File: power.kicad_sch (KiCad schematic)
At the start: 76 parts, among them J5 VJ1, Q1 BC857, Q2 2N7002, U1 LFE5U-85F-6BG381C, U3 TLV62569DBV, U4 TLV62569DBV, U5 TLV62569DBV

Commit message: updating part numbers across schematcs
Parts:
- C1, C11, C12, C3, C4, C5, C7, C8, C9: MPN CC0805ZKY5V5BB226 -> CC0805ZKY5V5BB226
- C26, C27, C28, C29, C30, C31, C32, C48, C49, C50, C51, C53: MPN CX0603MRX7R8BB223 -> CC0603JRX7R8BB223
- D10, D13, D14, D16, D17, D27: MPN 1N4148WS -> 1N4148WS
- R10: Digikey (none) -> 13-AC0603FR-07130RLCT-ND; MPN (none) -> 13-AC0603FR-07130RLCT-ND
- R6, R66, R8: Digikey (none) -> 13-AC0603FR-071K1LCT-ND; MPN (none) -> 13-AC0603FR-071K1LCT-ND
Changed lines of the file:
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@@
 			)
 		)
-		(property "MPN" "CC0805ZKY5V5BB226 "
+		(property "MPN" "CC0805ZKY5V5BB226"
 			(at 187.96 93.98 0)
 			(effects
@@
 			)
 		)
-		(property "MPN" "CC0805ZKY5V5BB226 "
+		(property "MPN" "CC0805ZKY5V5BB226"
 			(at 248.92 83.82 0)
 			(effects
@@
 			)
 		)
-		(property "MPN" "CC0805ZKY5V5BB226 "
+		(property "MPN" "CC0805ZKY5V5BB226"
 			(at 257.81 83.82 0)
 			(effects
@@
 			)
 		)
-		(property "MPN" "CC0805ZKY5V5BB226 "
+		(property "MPN" "CC0805ZKY5V5BB226"
 			(at 187.96 154.94 0)
 			(effects
@@
 			)
 		)
-		(property "MPN" "CC0805ZKY5V5BB226 "
+		(property "MPN" "CC0805ZKY5V5BB226"
 			(at 248.92 144.78 0)
 			(effects
@@
 			)
 		)
-		(property "MPN" "CC0805ZKY5V5BB226 "
+		(property "MPN" "CC0805ZKY5V5BB226"
 			(at 257.81 144.78 0)
 			(effects
@@
 			)
 		)
-		(property "MPN" "CC0805ZKY5V5BB226 "
+		(property "MPN" "CC0805ZKY5V5BB226"
 			(at 187.96 124.46 0)
 			(effects
@@
 			)
 		)
-		(property "MPN" "CC0805ZKY5V5BB226 "
+		(property "MPN" "CC0805ZKY5V5BB226"
 			(at 248.92 114.3 0)
 			(effects
@@
 			)
 		)
-		(property "MPN" "CC0805ZKY5V5BB226 "
+		(property "MPN" "CC0805ZKY5V5BB226"
 			(at 257.81 114.3 0)
 			(effects
@@
 			)
 		)
-		(property "MPN" "1N4148WS "
+		(property "MPN" "1N4148WS"
 			(at 109.22 107.95 0)
 			(effects
@@
 			)
 		)
+		(property "Digikey" "13-AC0603FR-071K1LCT-ND"
+			(at 86.36 95.25 90)
+			(effects
+				(font
+					(size 1.27 1.27)
+				)
+				(hide yes)
+			)
+		)
+		(property "MPN" "13-AC0603FR-071K1LCT-ND"
+			(at 86.36 95.25 90)
+			(effects
+				(font
+					(size 1.27 1.27)
+				)
+				(hide yes)
+			)
+		)
 		(pin "1"
 		)
@@
 			)
 		)
+		(property "Digikey" "13-AC0603FR-071K1LCT-ND"
+			(at 104.14 132.08 90)
+			(effects
+				(font
+					(size 1.27 1.27)
+				)
+				(hide yes)
+			)
+		)
+		(property "MPN" "13-AC0603FR-071K1LCT-ND"
+			(at 104.14 132.08 90)
+			(effects
+				(font
+					(size 1.27 1.27)
+				)
+				(hide yes)
+			)
+		)
 		(pin "1"
 		)
@@
 			)
 		)
-		(property "MPN" "1N4148WS "
+		(property "MPN" "1N4148WS"
 			(at 102.87 107.95 0)
 			(effects
@@
 			)
 		)
-		(property "MPN" "1N4148WS "
+		(property "MPN" "1N4148WS"
 			(at 86.36 137.16 0)
 			(effects
@@
 			)
 		)
-		(property "MPN" "1N4148WS "
+		(property "MPN" "1N4148WS"
 			(at 73.66 100.33 0)
 			(effects
@@
 			)
 		)
-		(property "MPN" "1N4148WS "
+		(property "MPN" "1N4148WS"
 			(at 80.01 105.41 0)
 			(effects
@@
 			)
 		)
+		(property "Digikey" "13-AC0603FR-07130RLCT-ND"
+			(at 68.58 125.73 90)
+			(effects
+				(font
+					(size 1.27 1.27)
+				)
+				(hide yes)
+			)
+		)
+		(property "MPN" "13-AC0603FR-07130RLCT-ND"
+			(at 68.58 125.73 90)
+			(effects
+				(font
+					(size 1.27 1.27)
+				)
+				(hide yes)
+			)
+		)
 		(pin "1"
 		)
@@
 			)
 		)
-		(property "MPN" "CX0603MRX7R8BB223"
+		(property "MPN" "CC0603JRX7R8BB223"
 			(at 153.67 120.65 0)
 			(effects
@@
 			)
 		)
-		(property "MPN" "CX0603MRX7R8BB223"
+		(property "MPN" "CC0603JRX7R8BB223"
 			(at 139.7 82.55 0)
 			(effects
@@
 			)
 		)
-		(property "MPN" "CX0603MRX7R8BB223"
+		(property "MPN" "CC0603JRX7R8BB223"
 			(at 146.05 82.55 0)
 			(effects
@@
 			)
 		)
-		(property "MPN" "CX0603MRX7R8BB223"
+		(property "MPN" "CC0603JRX7R8BB223"
 			(at 139.7 101.6 0)
 			(effects
@@
 			)
 		)
-		(property "MPN" "CX0603MRX7R8BB223"
+		(property "MPN" "CC0603JRX7R8BB223"
 			(at 146.05 101.6 0)
 			(effects
@@
 			)
 		)
-		(property "MPN" "CX0603MRX7R8BB223"
+		(property "MPN" "CC0603JRX7R8BB223"
 			(at 146.05 120.65 0)
 			(effects
@@
 			)
 		)
-		(property "MPN" "CX0603MRX7R8BB223"
+		(property "MPN" "CC0603JRX7R8BB223"
 			(at 139.7 120.65 0)
 			(effects
@@
 			)
 		)
-		(property "MPN" "CX0603MRX7R8BB223"
+		(property "MPN" "CC0603JRX7R8BB223"
 			(at 95.25 180.34 0)
 			(effects
@@
 			)
 		)
-		(property "MPN" "CX0603MRX7R8BB223"
+		(property "MPN" "CC0603JRX7R8BB223"
 			(at 82.55 180.34 0)
 			(effects
@@
 			)
 		)
-		(property "MPN" "CX0603MRX7R8BB223"
+		(property "MPN" "CC0603JRX7R8BB223"
 			(at 101.6 180.34 0)
 			(effects
@@
 			)
 		)
-		(property "MPN" "CX0603MRX7R8BB223"
+		(property "MPN" "CC0603JRX7R8BB223"
 			(at 88.9 180.34 0)
 			(effects
@@
 			)
 		)
-		(property "MPN" "CX0603MRX7R8BB223"
+		(property "MPN" "CC0603JRX7R8BB223"
 			(at 160.02 120.65 0)
 			(effects
@@
 			)
 		)
-		(property "MPN" "1N4148WS "
+		(property "MPN" "1N4148WS"
 			(at 73.66 90.17 0)
 			(effects
@@
 			)
 		)
+		(property "Digikey" "13-AC0603FR-071K1LCT-ND"
+			(at 80.01 83.82 90)
+			(effects
+				(font
+					(size 1.27 1.27)
+				)
+				(hide yes)
+			)
+		)
+		(property "MPN" "13-AC0603FR-071K1LCT-ND"
+			(at 80.01 83.82 90)
+			(effects
+				(font
+					(size 1.27 1.27)
+				)
+				(hide yes)
+			)
+		)

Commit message: update mouser PN for 4.8kresistor
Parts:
- R1, R3, R4, RB2: MPN AC0603FR-104K7L -> 603-RC0603FR-074K7L
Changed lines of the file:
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@@
 			)
 		)
-		(property "MPN" "AC0603FR-104K7L"
+		(property "MPN" "603-RC0603FR-074K7L"
 			(at 243.84 119.38 90)
 			(effects
@@
 			)
 		)
-		(property "MPN" "AC0603FR-104K7L"
+		(property "MPN" "603-RC0603FR-074K7L"
 			(at 109.22 119.38 90)
 			(effects
@@
 			)
 		)
-		(property "MPN" "AC0603FR-104K7L"
+		(property "MPN" "603-RC0603FR-074K7L"
 			(at 123.19 119.38 90)
 			(effects
@@
 			)
 		)
-		(property "MPN" "AC0603FR-104K7L"
+		(property "MPN" "603-RC0603FR-074K7L"
 			(at 80.01 111.76 90)
 			(effects

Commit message: update mpn at mouser/digikey for 2N7002
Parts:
- Q2: Digikey 2N7002K-TPMSCT-ND -> 2N7002ET1GOSCT-ND; LCSC C179727 -> C71533; MPN 2N7002P,215 -> 863-2N7002ET1G
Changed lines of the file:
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@@
 			)
 		)
-		(property "MPN" "2N7002P,215"
+		(property "MPN" "863-2N7002ET1G"
 			(at 101.6 142.24 0)
 			(effects
@@
 			)
 		)
-		(property "Digikey" "2N7002K-TPMSCT-ND"
+		(property "Digikey" "2N7002ET1GOSCT-ND"
 			(at 101.6 142.24 0)
 			(effects
@@
 			)
 		)
-		(property "LCSC" "C179727"
+		(property "LCSC" "C71533"
 			(at 101.6 142.24 0)
 			(effects

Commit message: switch from NSR0530HT1G  to BAT54WSQ-7-F
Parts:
- D12: MPN NSR0530HT1G -> BAT54WSQ-7-F; MPN2 (none) -> NSR0530HT1G
- D15: MPN NSR0530HT1G -> BAT54WSQ-7-F; MPN2 BAT54WSQ-7-F -> NSR0530HT1G
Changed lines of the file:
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@@
 			)
 		)
-		(property "MPN" "NSR0530HT1G "
+		(property "MPN" "BAT54WSQ-7-F"
 			(at 78.74 142.24 0)
 			(effects
@@
 			)
 		)
-		(property "MPN2" "BAT54WSQ-7-F "
+		(property "MPN2" "NSR0530HT1G "
 			(at 78.74 142.24 0)
 			(effects
@@
 			)
 		)
-		(property "MPN" "NSR0530HT1G "
+		(property "MPN" "BAT54WSQ-7-F"
+			(at 96.52 125.73 0)
+			(effects
+				(font
+					(size 1.27 1.27)
+				)
+				(hide yes)
+			)
+		)
+		(property "MPN2" "NSR0530HT1G "
 			(at 96.52 125.73 0)
 			(effects

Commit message: adjust mouser part number of BC857 to 757-TBC857BLM
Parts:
- Q1: MPN BC857 -> 757-TBC857BLM
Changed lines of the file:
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@@
 			)
 		)
-		(property "MPN" "BC857"
+		(property "MPN" "757-TBC857BLM"
 			(at 100.33 95.25 0)
 			(effects

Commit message: Remove 'Leave Empty' in favor of using attributes
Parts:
- J5, RP1, RP2, RP3, RV2: Note Leave empty -> (none); now not fitted
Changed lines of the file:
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@@
 		(on_board yes)
 		(in_pos_files yes)
-		(dnp no)
+		(dnp yes)
 		(property "Reference" "RP1"
 			(at 271.78 76.708 0)
@@
 			)
 		)
-		(property "Note" "Leave empty"
+		(property "Note" ""
 			(at 271.78 78.74 0)
 			(hide yes)
@@
 		(on_board yes)
 		(in_pos_files yes)
-		(dnp no)
+		(dnp yes)
 		(property "Reference" "RP2"
 			(at 271.78 107.188 0)
@@
 			)
 		)
-		(property "Note" "Leave empty"
+		(property "Note" ""
 			(at 271.78 109.22 0)
 			(hide yes)
@@
 		(on_board yes)
 		(in_pos_files yes)
-		(dnp no)
+		(dnp yes)
 		(property "Reference" "RP3"
 			(at 271.78 137.668 0)
@@
 			)
 		)
-		(property "Note" "Leave empty"
+		(property "Note" ""
 			(at 271.78 139.7 0)
 			(hide yes)
@@
 		(on_board yes)
 		(in_pos_files yes)
-		(dnp no)
+		(dnp yes)
 		(property "Reference" "J5"
 			(at 40.64 48.26 0)
@@
 			)
 		)
-		(property "Note" "Leave empty"
+		(property "Note" ""
 			(at 40.64 43.18 0)
 			(hide yes)
@@
 		(in_bom no)
 		(on_board yes)
-		(in_pos_files yes)
-		(dnp no)
+		(in_pos_files no)
+		(dnp yes)
 		(property "Reference" "RV2"
 			(at 20.32 46.99 0)
@@
 			)
 		)
-		(property "Note" "Leave empty"
+		(property "Note" ""
 			(at 22.86 46.99 0)
 			(hide yes)

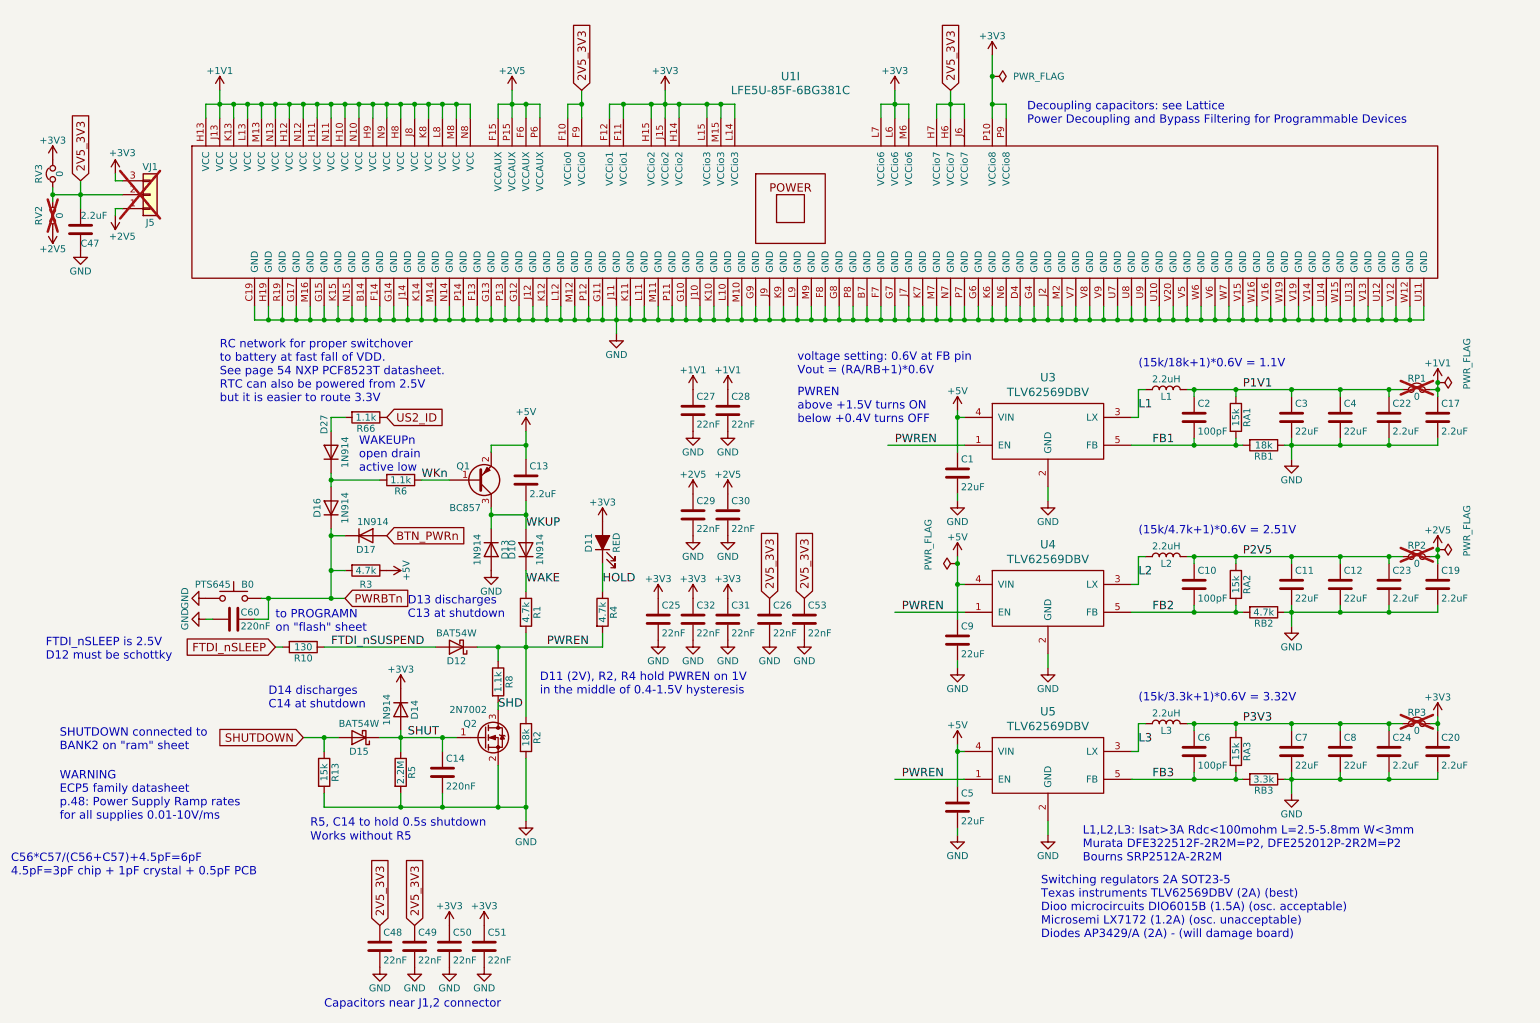
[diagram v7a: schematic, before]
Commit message: remove wake up/shutdown logic
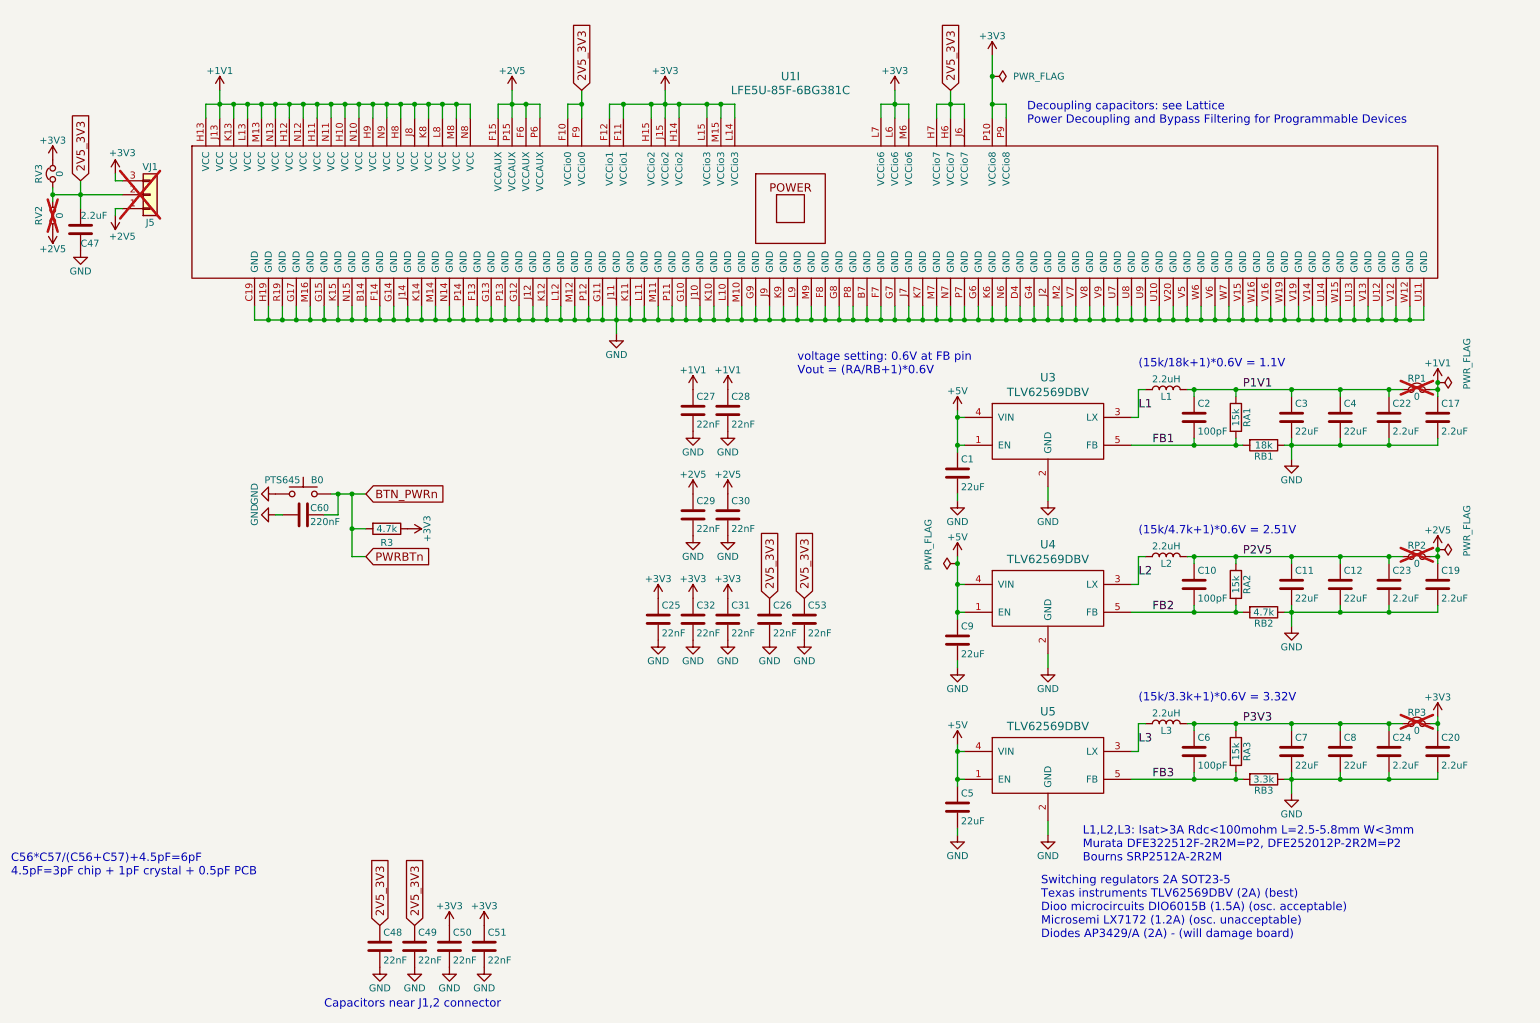
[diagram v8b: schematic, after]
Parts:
- removed C13: 2.2uF, Capacitor_SMD:C_0805_2012Metric, symbol Device:C
- removed C14: 220nF, Capacitor_SMD:C_0603_1608Metric, symbol Device:C
- removed D10, D13, D14, D16, D17, D27: 1N914, Diode_SMD:D_SOD-323_HandSoldering, symbol Device:D
- removed D11: RED, LED_SMD:LED_0805_2012Metric, symbol Device:LED_ALT
- removed D12, D15: BAT54W, Diode_SMD:D_SOD-323_HandSoldering, symbol Device:D_Schottky
- removed Q1: BC857, Package_TO_SOT_SMD:SOT-23, symbol Device:Q_PNP_BEC
- removed Q2: 2N7002, Package_TO_SOT_SMD:SOT-23, symbol Device:Q_NMOS_GSD
- removed R1, R4: 4.7k, Resistor_SMD:R_0603_1608Metric, symbol Device:R
- removed R10: 130, Resistor_SMD:R_0603_1608Metric, symbol Device:R
- removed R13: 15k, Resistor_SMD:R_0603_1608Metric, symbol Device:R
- removed R2: 18k, Resistor_SMD:R_0603_1608Metric, symbol Device:R
- removed R5: 2.2M, Resistor_SMD:R_0603_1608Metric, symbol Device:R
- removed R6, R66, R8: 1.1k, Resistor_SMD:R_0603_1608Metric, symbol Device:R
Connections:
- net PWRBTn is gone; now on net BTN_PWRn: B0.1, C60.1, R3.2
- net PWREN is gone; now on net +5V: U3.1 (EN), U4.1 (EN), U5.1 (EN)
- net +3V3: now also R3.1
- net +5V: no longer R3.1
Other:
- note removed: "D11 (2V), R2, R4 hold PWREN on 1V in the middle of 0.4-1.5V hysteresis"
- note removed: "D13 discharges C13 at shutdown"
- note removed: "D14 discharges C14 at shutdown"
- note removed: "FTDI_nSLEEP is 2.5V D12 must be schottky"
- note removed: "PWREN above +1.5V turns ON below +0.4V turns OFF"
- note removed: "R5, C14 to hold 0.5s shutdown"
- note removed: "RC network for proper switchover to battery at fast fall of VDD. See page 54 NXP PCF8523T datasheet. RTC can also be powered from 2.5V but it is easier to route 3.3V"
- note removed: "SHUTDOWN connected to BANK2 on "ram" sheet"
- note removed: "WAKEUPn open drain active low"
- note removed: "WARNING ECP5 family datasheet p.48: Power Supply Ramp rates for all supplies 0.01-10V/ms"
- note removed: "Works without R5"
- note removed: "to PROGRAMN on "flash" sheet"
- moved on the sheet: B0, C60, R3
